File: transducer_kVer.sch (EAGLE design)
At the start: 12 parts, among them U1 ADS1014IDGST

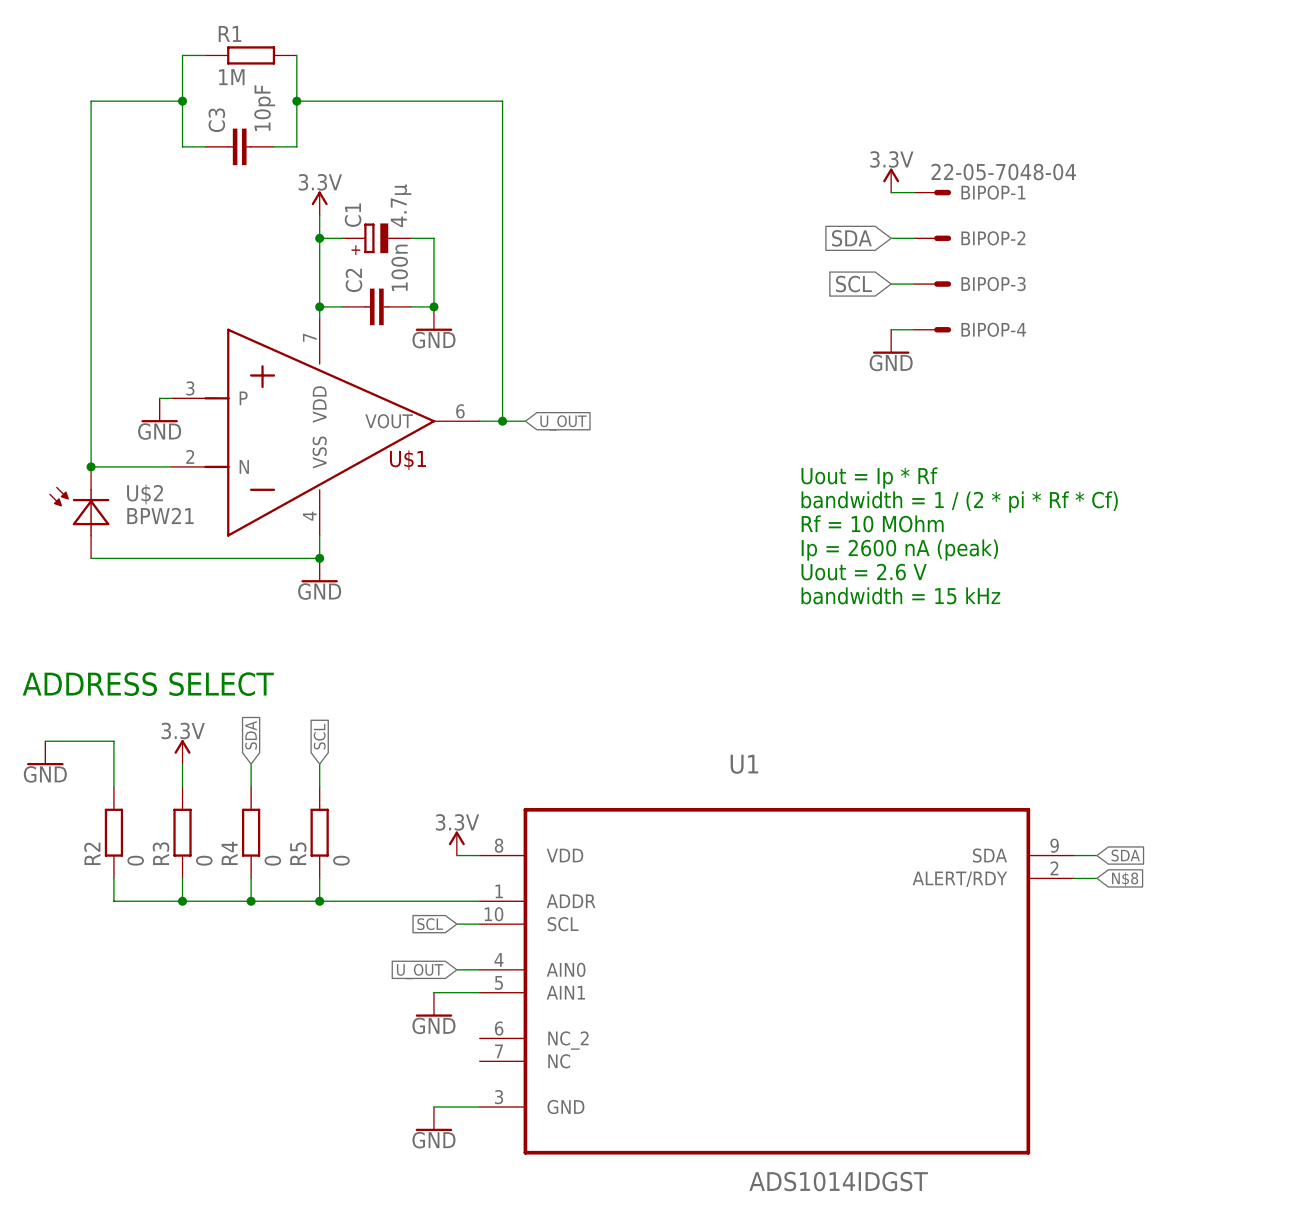
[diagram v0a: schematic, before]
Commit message: BIPOP board redesigned, new versions of transducers added.
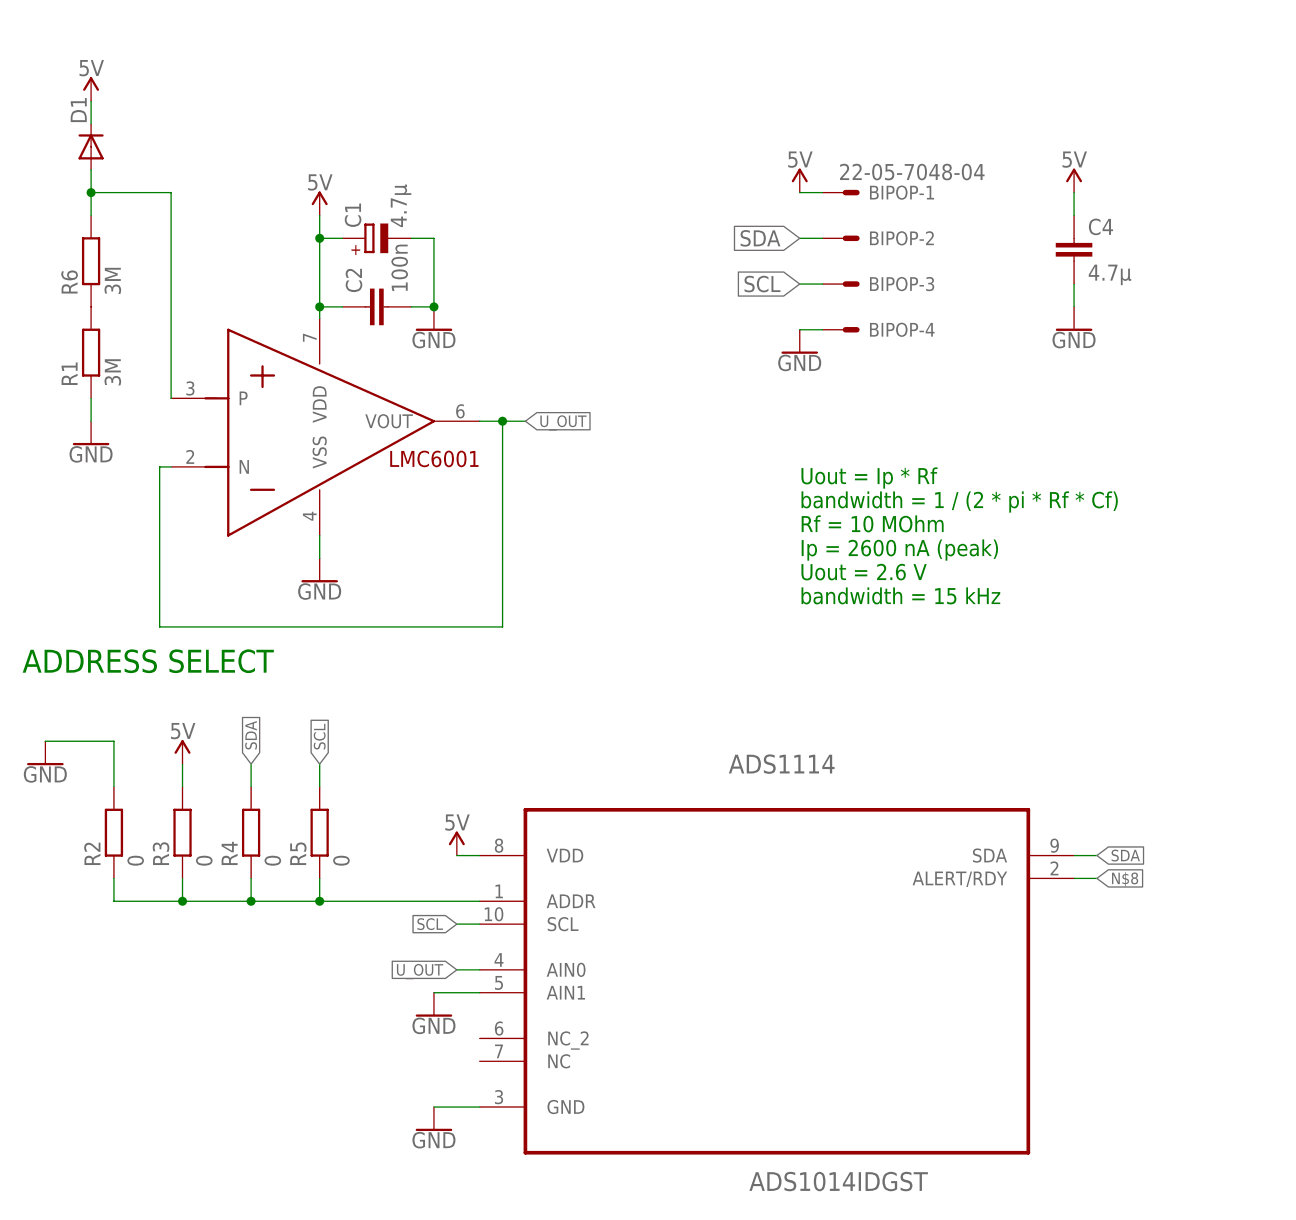
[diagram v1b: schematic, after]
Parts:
- removed C3: 10pF, rcl:C-EUC0603
- removed U$2: BPW21, customy:BPW21
- added C4: 4.7µ, rcl:C-EUC0805
- added D1: (no value), diode:DIODE-TO18D
- added R6: 3M, rcl:R-EU_R0805
- R1: value 1M -> 3M
- renumbered U$1 to LMC6001, U1 to ADS1114
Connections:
- net N$3 renamed ADR
- removed net 3.3V: ADS1114.VDD, BIPOP-1.S, C1.+, C2.1, LMC6001.VDD, R3.2
- removed net N$5: C3.1, LMC6001.N, R1.1, U$2.C
- new net 5V: ADS1114.VDD, BIPOP-1.S, C1.+, C2.1, C4.1, D1.C, LMC6001.VDD, R3.2
- new net N$2: R1.2, R6.1
- new net N$3: D1.A, LMC6001.P, R6.2
- net GND: now also C4.2, R1.1; no longer LMC6001.P, U$2.A
- net U_OUT: now also LMC6001.N; no longer C3.2, R1.2
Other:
- moved on the sheet: BIPOP-1, BIPOP-2, BIPOP-3, BIPOP-4, R1
